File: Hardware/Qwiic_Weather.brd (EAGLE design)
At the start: 25.4 x 25.4 mm, 48 parts, among them J1 QWIIC, J2 QWIIC, J3 PTH, U1 BME280

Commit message: changes during checklist run 1
-moved all text in sch to vector
-removed unwanted value on jumper
-4pin pth connector replaced with sparkfun library
-vcc range added
-dimension width to 8 mils
-updated package on IC to fatten up silk width
-measures to inch
-Designer added to tdocu in brd
-nudged via to avoid silk on I2C label
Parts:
- J3: device SparkX:1X04_NO_SILK -> SparkFun-Connectors:1X04_NO_SILK
- SJ1: value JUMPER-SMT_3_2-NC_TRACE_NO-SILK -> (none)
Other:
- board text added: "Kenny Hora, Pete Lewis"
- board text removed: "Measurements in mm"
- board text removed: "Pete Lewis"
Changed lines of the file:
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@@
 <?xml version="1.0" encoding="utf-8"?>
 <!DOCTYPE eagle SYSTEM "eagle.dtd">
-<eagle version="9.4.0">
+<eagle version="9.4.2">
 <drawing>
 <settings>
@@
 <board>
 <plain>
-<wire x1="0" y1="0" x2="0" y2="25.4" width="0.3048" layer="20"/>
-<wire x1="0" y1="25.4" x2="25.4" y2="25.4" width="0.3048" layer="20"/>
-<wire x1="25.4" y1="25.4" x2="25.4" y2="0" width="0.3048" layer="20"/>
-<wire x1="25.4" y1="0" x2="0" y2="0" width="0.3048" layer="20"/>
+<wire x1="0" y1="0" x2="0" y2="25.4" width="0.2032" layer="20"/>
+<wire x1="0" y1="25.4" x2="25.4" y2="25.4" width="0.2032" layer="20"/>
+<wire x1="25.4" y1="25.4" x2="25.4" y2="0" width="0.2032" layer="20"/>
+<wire x1="25.4" y1="0" x2="0" y2="0" width="0.2032" layer="20"/>
 <text x="24.511" y="12.827" size="1.016" layer="16" font="vector" ratio="20" rot="SMR270" align="center">v10</text>
-<text x="16.51" y="-21.59" size="1.778" layer="51">Pete Lewis</text>
+<text x="16.51" y="-21.59" size="1.778" layer="51">Kenny Hora, Pete Lewis</text>
 <text x="8.509" y="10.414" size="0.6096" layer="25">CCS811</text>
 <text x="14.859" y="10.541" size="0.6096" layer="25">BME280</text>
-<dimension x1="0" y1="0" x2="25.4" y2="0" x3="12.7" y3="-3.81" textsize="1.778" layer="47"/>
-<dimension x1="0" y1="0" x2="0" y2="25.4" x3="-5.08" y3="12.7" textsize="1.778" layer="47"/>
-<dimension x1="5.08" y1="1.27" x2="0" y2="1.27" x3="2.54" y3="-7.62" textsize="1.778" layer="47"/>
-<dimension x1="2.54" y1="22.86" x2="2.54" y2="0" x3="-1.27" y3="11.43" textsize="1.778" layer="47"/>
-<dimension x1="2.54" y1="22.86" x2="0" y2="22.86" x3="1.27" y3="26.67" textsize="1.778" layer="47"/>
-<dimension x1="22.86" y1="22.86" x2="0" y2="22.86" x3="11.43" y3="30.48" textsize="1.778" layer="47"/>
-<text x="-1.27" y="-12.7" size="1.778" layer="47">Measurements in mm</text>
+<dimension x1="0" y1="0" x2="25.4" y2="0" x3="12.7" y3="-3.81" textsize="1.778" layer="47" unit="inch" visible="yes"/>
+<dimension x1="0" y1="0" x2="0" y2="25.4" x3="-5.08" y3="12.7" textsize="1.778" layer="47" unit="inch" visible="yes"/>
+<dimension x1="5.08" y1="1.27" x2="0" y2="1.27" x3="2.54" y3="-7.62" textsize="1.778" layer="47" unit="inch" visible="yes"/>
+<dimension x1="2.54" y1="22.86" x2="2.54" y2="0" x3="-1.27" y3="11.43" textsize="1.778" layer="47" unit="inch" visible="yes"/>
+<dimension x1="2.54" y1="22.86" x2="0" y2="22.86" x3="1.27" y3="26.67" textsize="1.778" layer="47" unit="inch" visible="yes"/>
+<dimension x1="22.86" y1="22.86" x2="0" y2="22.86" x3="11.43" y3="30.48" textsize="1.778" layer="47" unit="inch" visible="yes"/>
 </plain>
 <attributes>
@@
 <attribute name="VALUE" x="2.54" y="20.828" size="0.6096" layer="27" font="vector" ratio="20" align="top-center"/>
 </element>
-<element name="SJ1" library="SparkFun-Jumpers" package="SMT-JUMPER_3_2-NC_TRACE_NO-SILK" value="JUMPER-SMT_3_2-NC_TRACE_NO-SILK" x="7.62" y="8.89" smashed="yes" rot="MR180">
+<element name="SJ1" library="SparkFun-Jumpers" package="SMT-JUMPER_3_2-NC_TRACE_NO-SILK" value="" x="7.62" y="8.89" smashed="yes" rot="MR180">
 <attribute name="NAME" x="7.62" y="7.747" size="0.6096" layer="26" font="vector" ratio="20" rot="MR180" align="bottom-center"/>
 <attribute name="VALUE" x="7.62" y="10.033" size="0.6096" layer="28" font="vector" ratio="20" rot="MR180" align="top-center"/>
@@
 <attribute name="VALUE" x="23.622" y="11.049" size="0.6096" layer="27" font="vector" ratio="20" rot="R90"/>
 </element>
-<element name="J3" library="SparkX" package="1X04_NO_SILK" value="PTH" x="6.35" y="1.27" smashed="yes">
+<element name="J3" library="SparkFun-Connectors" package="1X04_NO_SILK" value="PTH" x="6.35" y="1.27" smashed="yes">
 <attribute name="NAME" x="5.08" y="2.667" size="0.6096" layer="25" font="vector" ratio="20"/>
 <attribute name="VALUE" x="5.08" y="-0.762" size="0.6096" layer="27" font="vector" ratio="20"/>
@@
 <contactref element="U1" pad="4"/>
 <wire x1="5.08" y1="11.2" x2="6.5024" y2="11.2" width="0.3048" layer="1"/>
-<wire x1="6.7818" y1="11.4794" x2="6.5024" y2="11.2" width="0.3048" layer="1"/>
-<wire x1="7.6214" y1="11.4794" x2="6.7818" y2="11.4794" width="0.3048" layer="1"/>
-<wire x1="7.62" y1="11.478" x2="7.6214" y2="11.4794" width="0.3048" layer="1"/>
-<wire x1="7.62" y1="9.74" x2="7.62" y2="11.478" width="0.3048" layer="1"/>
+<wire x1="6.8834" y1="11.581" x2="6.5024" y2="11.2" width="0.3048" layer="1"/>
+<wire x1="7.6214" y1="11.581" x2="6.8834" y2="11.581" width="0.3048" layer="1"/>
+<wire x1="7.62" y1="11.5796" x2="7.6214" y2="11.581" width="0.3048" layer="1"/>
+<wire x1="7.62" y1="9.74" x2="7.62" y2="11.5796" width="0.3048" layer="1"/>
 <wire x1="11.675" y1="13.675" x2="9.3824" y2="13.675" width="0.3048" layer="1"/>
 <wire x1="9.3824" y1="13.675" x2="9.3726" y2="13.6652" width="0.3048" layer="1"/>
 <via x="9.3726" y="13.6652" extent="1-16" drill="0.381"/>
-<via x="7.6214" y="11.4794" extent="1-16" drill="0.381"/>
+<via x="7.6214" y="11.581" extent="1-16" drill="0.381"/>
 <wire x1="13.97" y1="1.27" x2="13.97" y2="8.9916" width="0.3048" layer="1"/>
 <wire x1="13.97" y1="8.9916" x2="12.8778" y2="10.0838" width="0.3048" layer="1"/>
@@
 <wire x1="13.843" y1="15.367" x2="13.843" y2="11.2522" width="0.3048" layer="16"/>
 <wire x1="13.843" y1="11.2522" x2="12.8778" y2="10.287" width="0.3048" layer="16"/>
-<wire x1="7.6214" y1="11.4794" x2="7.7244" y2="11.5824" width="0.3048" layer="16"/>
+<wire x1="7.6214" y1="11.581" x2="7.6228" y2="11.5824" width="0.3048" layer="16"/>
 <wire x1="9.3726" y1="13.6652" x2="9.3726" y2="11.6078" width="0.3048" layer="16"/>
 <wire x1="9.3472" y1="11.5824" x2="11.5824" y2="11.5824" width="0.3048" layer="16"/>
 <wire x1="9.3726" y1="11.6078" x2="9.3472" y2="11.5824" width="0.3048" layer="16"/>
-<wire x1="9.3472" y1="11.5824" x2="7.7244" y2="11.5824" width="0.3048" layer="16"/>
+<wire x1="9.3472" y1="11.5824" x2="7.6228" y2="11.5824" width="0.3048" layer="16"/>
 </signal>
 <signal name="SDI/SDA">
@@
 <wire x1="11.0236" y1="9.4234" x2="10.9982" y2="9.4488" width="0.3048" layer="16"/>
 <via x="10.9982" y="9.4488" extent="1-16" drill="0.381"/>
-<wire x1="9.07303125" y1="12.2" x2="5.08" y2="12.2" width="0.3048" layer="1"/>
-<wire x1="9.89803125" y1="13.025" x2="9.2202" y2="12.34716875" width="0.3048" layer="1"/>
-<wire x1="11.675" y1="13.025" x2="9.89803125" y2="13.025" width="0.3048" layer="1"/>
-<wire x1="9.2202" y1="9.74" x2="9.2202" y2="12.34716875" width="0.3048" layer="1"/>
-<wire x1="9.07303125" y1="12.2" x2="9.2202" y2="12.34716875" width="0.3048" layer="1"/>
+<wire x1="5.08" y1="12.2" x2="6.8914" y2="12.2" width="0.3048" layer="1"/>
+<wire x1="9.66943125" y1="13.025" x2="9.2202" y2="12.57576875" width="0.3048" layer="1"/>
+<wire x1="11.675" y1="13.025" x2="9.66943125" y2="13.025" width="0.3048" layer="1"/>
+<wire x1="9.2202" y1="9.74" x2="9.2202" y2="12.57576875" width="0.3048" layer="1"/>
+<wire x1="7.26716875" y1="12.57576875" x2="9.2202" y2="12.57576875" width="0.3048" layer="1"/>
+<wire x1="6.8914" y1="12.2" x2="7.26716875" y2="12.57576875" width="0.3048" layer="1"/>
 </signal>
 <signal name="3.3V">

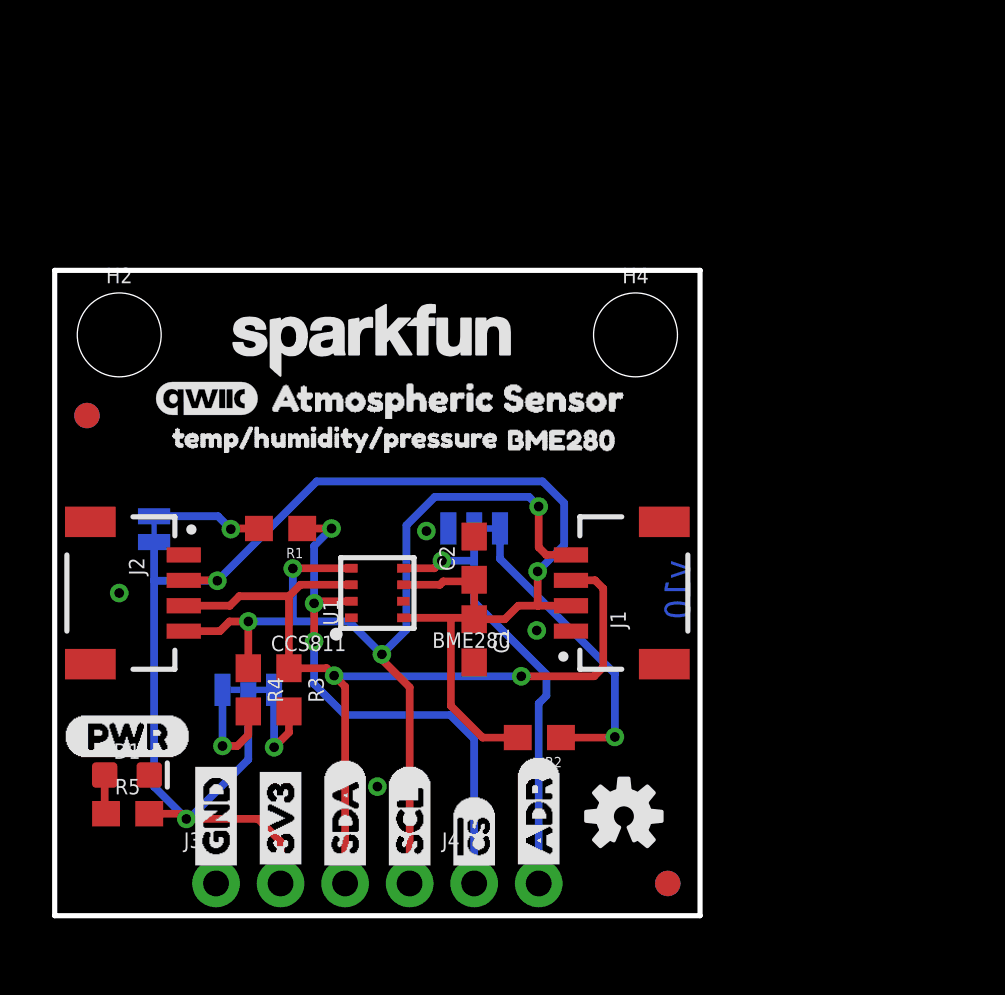
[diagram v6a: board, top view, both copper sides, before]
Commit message: Changes during/post group design review
-added power led disable jumper (and buzzard label and schematic text note).
-switched CS to "pointer" flag label cuz it's an input.
-added GND vias and nudges vias for better ground flow.
-changed info line to short dash.
-added text name for bottom half of schematic.
-moved fids added third standoff.
-Capitalized Temp Humidity Pressure text.
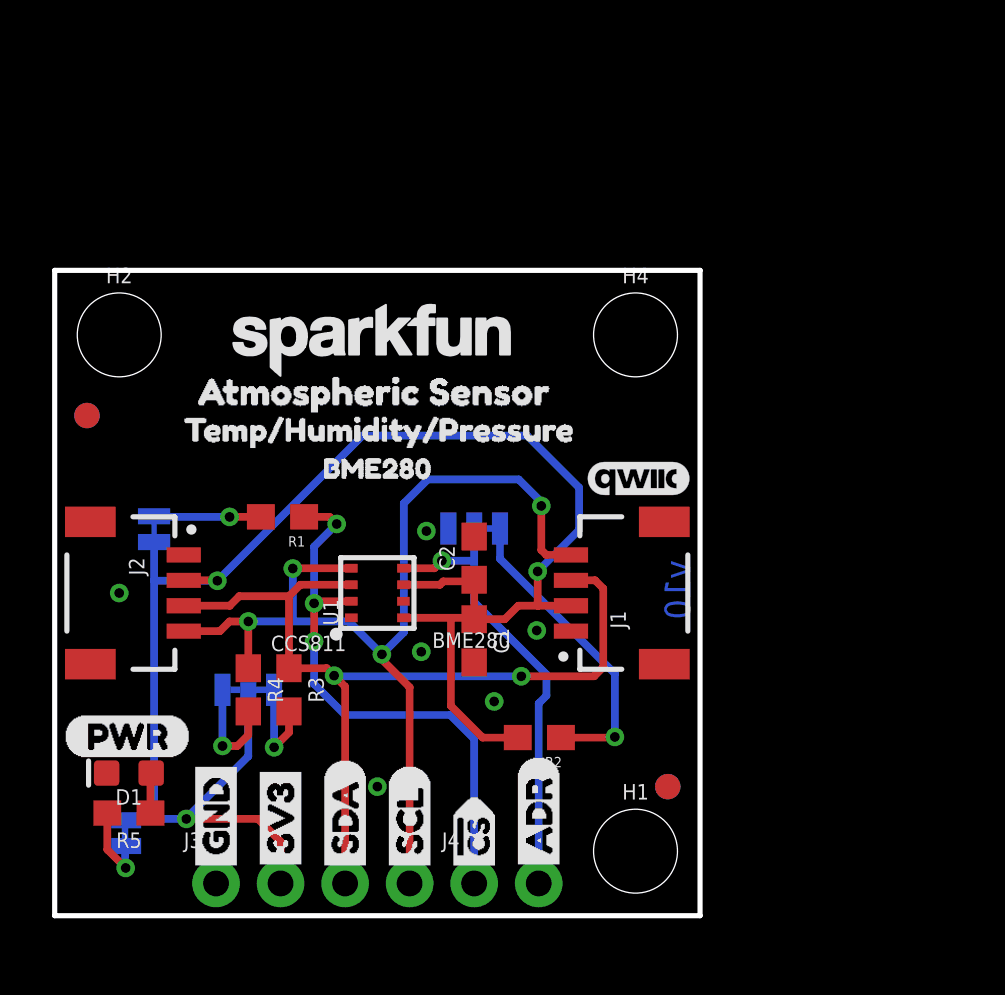
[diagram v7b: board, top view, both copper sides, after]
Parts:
- removed U$12: (no value), buzzard_labels:#CS7
- added H1: STAND-OFF, SparkFun-Hardware:STAND-OFF
- added JP1: (no value), SparkFun-Jumpers:SMT-JUMPER_2_NC_TRACE_NO-SILK
- added U$23: (no value), buzzard_labels (3):TEMP#HUMIDITY#PRESSURE0
- added U$24: (no value), buzzard_labels (4):#CS0
- U$1: device buzzard_labels:#CS7 -> buzzard_labels (5):LED0
- U$14: device buzzard_labels (2):TEMP#HUMIDITY#PRESSURE3 -> buzzard_labels (4):#CS0
- moved U$14 21.6 mm to (16.5, 1.30), turned to 90 degrees
- moved LOGO4 18.8 mm to (12.9, 20.1), flipped to the bottom
- moved U$16 17.3 mm to (23.0, 17.2)
- moved U$1 15.8 mm to (1.22, 5.41), flipped to the bottom, turned to 270 degrees
- moved U$15 7.32 mm to (9.88, 17.6)
- moved FD2 3.81 mm to (24.1, 5.08)
- moved FD3 3.81 mm to (24.1, 5.08)
- moved U$17 2.93 mm to (4.72, 20.6)
- moved R1 0.46 mm to (8.97, 15.7)
- moved D1 0.11 mm to (2.92, 5.61), turned to 180 degrees
- moved R5 0.06 mm to (2.92, 4.04), turned to 180 degrees
- renumbered SJ1 to JP4, SJ2 to JP2, SJ3 to JP3
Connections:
- new net N$7: JP1.1, R5.2
- net 3.3V: now also JP1.2; no longer R5.2
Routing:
- net N$7: track 0.00 -> 3.33 mm, vias 0 -> 1
- net 3.3V: track 66.6 -> 69.6 mm
- net SCK/SCL: track 38.5 -> 39.8 mm
- net !CS: track 21.9 -> 22.4 mm

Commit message: Post double-check changes
-added IO warning in schematic
-removed leftover CCS811 text object in tNames
-designer name to vector
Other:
- board text removed: "BME280"
- board text removed: "CCS811"
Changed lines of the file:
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@@
 <layer number="45" name="Holes" color="7" fill="1" visible="yes" active="yes"/>
 <layer number="46" name="Milling" color="3" fill="1" visible="no" active="yes"/>
-<layer number="47" name="Measures" color="7" fill="1" visible="yes" active="yes"/>
+<layer number="47" name="Measures" color="7" fill="1" visible="no" active="yes"/>
 <layer number="48" name="Document" color="7" fill="1" visible="no" active="yes"/>
 <layer number="49" name="Reference" color="7" fill="1" visible="yes" active="yes"/>
@@
 <wire x1="25.4" y1="0" x2="0" y2="0" width="0.2032" layer="20"/>
 <text x="24.511" y="12.827" size="1.016" layer="16" font="vector" ratio="20" rot="SMR270" align="center">v10</text>
-<text x="16.51" y="-21.59" size="1.778" layer="51">Kenny Hora, Pete Lewis</text>
-<text x="8.509" y="10.414" size="0.6096" layer="25">CCS811</text>
-<text x="14.859" y="10.541" size="0.6096" layer="25">BME280</text>
+<text x="16.51" y="-21.59" size="1.778" layer="51" font="vector">Kenny Hora, Pete Lewis</text>
 <dimension x1="0" y1="0" x2="25.4" y2="0" x3="12.7" y3="-3.81" textsize="1.778" layer="47" unit="inch" visible="yes"/>
 <dimension x1="0" y1="0" x2="0" y2="25.4" x3="-5.08" y3="12.7" textsize="1.778" layer="47" unit="inch" visible="yes"/>
